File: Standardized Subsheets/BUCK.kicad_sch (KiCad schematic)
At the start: 11 parts, among them U2 TPS562200

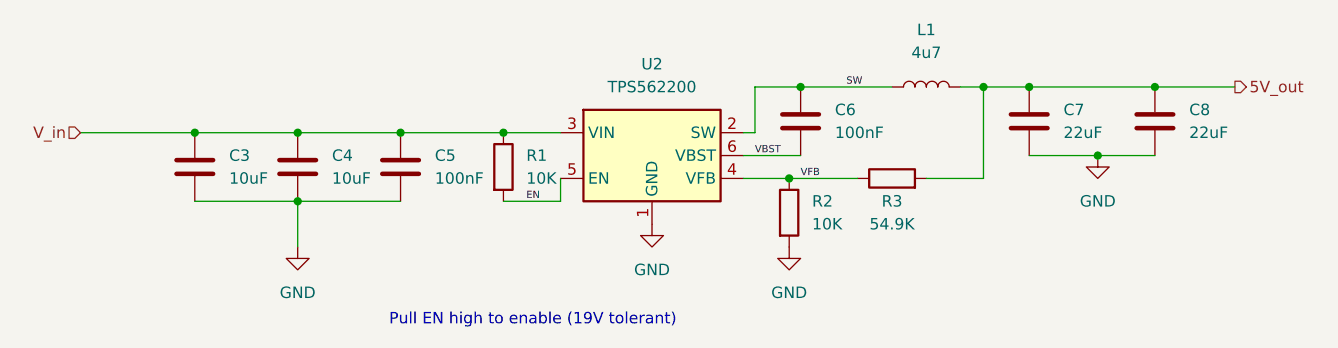
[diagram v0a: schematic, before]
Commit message: Updated VRMs to be 24V compliant
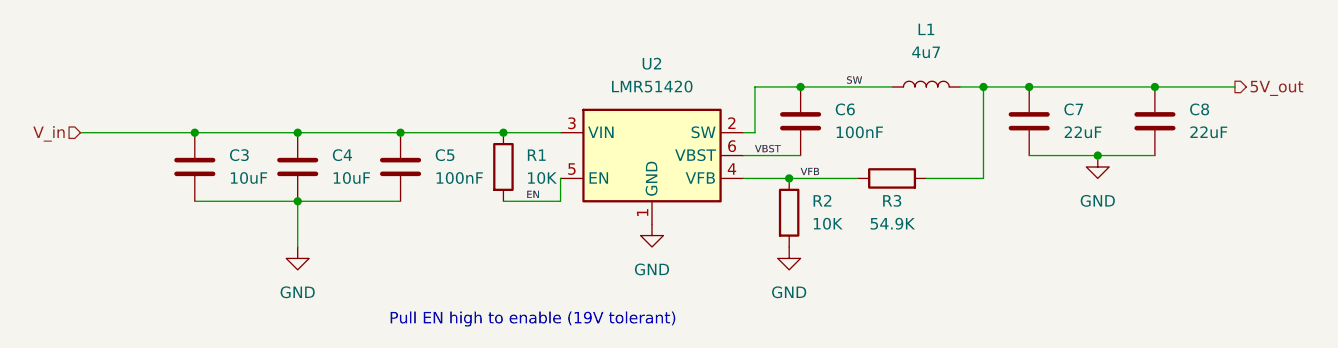
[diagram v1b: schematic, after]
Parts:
- U2: value TPS562200 -> LMR51420
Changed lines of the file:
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@@
     (in_bom yes) (on_board yes) (fields_autoplaced)
     (property "Reference" "U2" (id 0) (at 143.51 71.755 0))
-    (property "Value" "TPS562200" (id 1) (at 143.51 74.295 0))
+    (property "Value" "LMR51420" (id 1) (at 143.51 74.295 0))
     (property "Footprint" "Package_TO_SOT_SMD:SOT-23-6" (id 2) (at 144.78 88.265 0)
       (effects (font (size 1.27 1.27)) (justify left) hide)
     )
-    (property "Datasheet" "http://www.ti.com/lit/ds/symlink/tps563200.pdf" (id 3) (at 143.51 81.915 0)
+    (property "Datasheet" "https://www.ti.com/lit/ds/symlink/lmr51420.pdf?ts=1667094809731&ref_url=https%253A%252F%252Fwww.ti.com%252Fproduct%252FLMR51420" (id 3) (at 143.51 81.915 0)
       (effects (font (size 1.27 1.27)) hide)
     )

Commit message: gitignore
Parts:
- renumbered C3 to C15, C4 to C16, C5 to C17, C6 to C18, C7 to C19, C8 to C20, L1 to L2, R1 to R22, R2 to R23, R3 to R24, U2 to U6
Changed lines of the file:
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@@
     (effects (font (size 1.27 1.27)) (justify right))
   )
-  (symbol (lib_id "Device:C") (at 199.39 78.105 0)
-    (in_bom yes) (on_board yes) (fields_autoplaced)
-    (property "Reference" "C8" (id 0) (at 203.2 76.8349 0)
+  (symbol (lib_id "Device:C") (at 199.39 78.105 0) (unit 1)
+    (in_bom yes) (on_board yes) (fields_autoplaced)
+    (property "Reference" "C20" (id 0) (at 203.2 76.8349 0)
       (effects (font (size 1.27 1.27)) (justify left))
     )
@@
     (pin "2")
   )
-  (symbol (lib_id "power:GND") (at 193.04 81.915 0)
-    (in_bom yes) (on_board yes) (fields_autoplaced)
-    (property "Reference" "#PWR07" (id 0) (at 193.04 88.265 0)
+  (symbol (lib_id "power:GND") (at 193.04 81.915 0) (unit 1)
+    (in_bom yes) (on_board yes) (fields_autoplaced)
+    (property "Reference" "#PWR062" (id 0) (at 193.04 88.265 0)
       (effects (font (size 1.27 1.27)) hide)
     )
@@
     (pin "1")
   )
-  (symbol (lib_id "Device:C") (at 185.42 78.105 0)
-    (in_bom yes) (on_board yes) (fields_autoplaced)
-    (property "Reference" "C7" (id 0) (at 189.23 76.8349 0)
+  (symbol (lib_id "Device:C") (at 185.42 78.105 0) (unit 1)
+    (in_bom yes) (on_board yes) (fields_autoplaced)
+    (property "Reference" "C19" (id 0) (at 189.23 76.8349 0)
       (effects (font (size 1.27 1.27)) (justify left))
     )
@@
     (pin "2")
   )
-  (symbol (lib_id "Device:C") (at 92.71 83.185 0)
-    (in_bom yes) (on_board yes) (fields_autoplaced)
-    (property "Reference" "C3" (id 0) (at 96.52 81.9149 0)
+  (symbol (lib_id "Device:C") (at 92.71 83.185 0) (unit 1)
+    (in_bom yes) (on_board yes) (fields_autoplaced)
+    (property "Reference" "C15" (id 0) (at 96.52 81.9149 0)
       (effects (font (size 1.27 1.27)) (justify left))
     )
@@
     (pin "2")
   )
-  (symbol (lib_id "Device:C") (at 104.14 83.185 0)
-    (in_bom yes) (on_board yes) (fields_autoplaced)
-    (property "Reference" "C4" (id 0) (at 107.95 81.9149 0)
+  (symbol (lib_id "Device:C") (at 104.14 83.185 0) (unit 1)
+    (in_bom yes) (on_board yes) (fields_autoplaced)
+    (property "Reference" "C16" (id 0) (at 107.95 81.9149 0)
       (effects (font (size 1.27 1.27)) (justify left))
     )
@@
     (pin "2")
   )
-  (symbol (lib_id "Device:C") (at 115.57 83.185 0)
-    (in_bom yes) (on_board yes) (fields_autoplaced)
-    (property "Reference" "C5" (id 0) (at 119.38 81.9149 0)
+  (symbol (lib_id "Device:C") (at 115.57 83.185 0) (unit 1)
+    (in_bom yes) (on_board yes) (fields_autoplaced)
+    (property "Reference" "C17" (id 0) (at 119.38 81.9149 0)
       (effects (font (size 1.27 1.27)) (justify left))
     )
@@
     (pin "2")
   )
-  (symbol (lib_id "power:GND") (at 143.51 89.535 0)
-    (in_bom yes) (on_board yes) (fields_autoplaced)
-    (property "Reference" "#PWR05" (id 0) (at 143.51 95.885 0)
+  (symbol (lib_id "power:GND") (at 143.51 89.535 0) (unit 1)
+    (in_bom yes) (on_board yes) (fields_autoplaced)
+    (property "Reference" "#PWR060" (id 0) (at 143.51 95.885 0)
       (effects (font (size 1.27 1.27)) hide)
     )
@@
     (pin "1")
   )
-  (symbol (lib_id "Device:R") (at 170.18 84.455 90)
+  (symbol (lib_id "Device:R") (at 170.18 84.455 90) (unit 1)
     (in_bom yes) (on_board yes)
-    (property "Reference" "R3" (id 0) (at 170.18 86.995 90))
+    (property "Reference" "R24" (id 0) (at 170.18 86.995 90))
     (property "Value" "54.9K" (id 1) (at 170.18 89.535 90))
     (property "Footprint" "Resistor_SMD:R_0603_1608Metric_Pad0.98x0.95mm_HandSolder" (id 2) (at 170.18 86.233 90)
@@
     (pin "2")
   )
-  (symbol (lib_id "Device:R") (at 127 83.185 0)
-    (in_bom yes) (on_board yes) (fields_autoplaced)
-    (property "Reference" "R1" (id 0) (at 129.54 81.9149 0)
+  (symbol (lib_id "Device:R") (at 127 83.185 0) (unit 1)
+    (in_bom yes) (on_board yes) (fields_autoplaced)
+    (property "Reference" "R22" (id 0) (at 129.54 81.9149 0)
       (effects (font (size 1.27 1.27)) (justify left))
     )
@@
     (pin "2")
   )
-  (symbol (lib_id "power:GND") (at 158.75 92.075 0)
-    (in_bom yes) (on_board yes) (fields_autoplaced)
-    (property "Reference" "#PWR06" (id 0) (at 158.75 98.425 0)
+  (symbol (lib_id "power:GND") (at 158.75 92.075 0) (unit 1)
+    (in_bom yes) (on_board yes) (fields_autoplaced)
+    (property "Reference" "#PWR061" (id 0) (at 158.75 98.425 0)
       (effects (font (size 1.27 1.27)) hide)
     )
@@
     (pin "1")
   )
-  (symbol (lib_id "Regulator_Switching:TPS562200") (at 143.51 81.915 0)
-    (in_bom yes) (on_board yes) (fields_autoplaced)
-    (property "Reference" "U2" (id 0) (at 143.51 71.755 0))
+  (symbol (lib_id "Regulator_Switching:TPS562200") (at 143.51 81.915 0) (unit 1)
+    (in_bom yes) (on_board yes) (fields_autoplaced)
+    (property "Reference" "U6" (id 0) (at 143.51 71.755 0))
     (property "Value" "LMR51420" (id 1) (at 143.51 74.295 0))
     (property "Footprint" "Package_TO_SOT_SMD:SOT-23-6" (id 2) (at 144.78 88.265 0)
@@
     (pin "6")
   )
-  (symbol (lib_id "Device:C") (at 160.02 78.105 0)
-    (in_bom yes) (on_board yes) (fields_autoplaced)
-    (property "Reference" "C6" (id 0) (at 163.83 76.8349 0)
+  (symbol (lib_id "Device:C") (at 160.02 78.105 0) (unit 1)
+    (in_bom yes) (on_board yes) (fields_autoplaced)
+    (property "Reference" "C18" (id 0) (at 163.83 76.8349 0)
       (effects (font (size 1.27 1.27)) (justify left))
     )
@@
     (pin "2")
   )
-  (symbol (lib_id "Device:R") (at 158.75 88.265 0)
-    (in_bom yes) (on_board yes) (fields_autoplaced)
-    (property "Reference" "R2" (id 0) (at 161.29 86.9949 0)
+  (symbol (lib_id "Device:R") (at 158.75 88.265 0) (unit 1)
+    (in_bom yes) (on_board yes) (fields_autoplaced)
+    (property "Reference" "R23" (id 0) (at 161.29 86.9949 0)
       (effects (font (size 1.27 1.27)) (justify left))
     )
@@
     (pin "2")
   )
-  (symbol (lib_id "Device:L") (at 173.99 74.295 90)
-    (in_bom yes) (on_board yes) (fields_autoplaced)
-    (property "Reference" "L1" (id 0) (at 173.99 67.945 90))
+  (symbol (lib_id "Device:L") (at 173.99 74.295 90) (unit 1)
+    (in_bom yes) (on_board yes) (fields_autoplaced)
+    (property "Reference" "L2" (id 0) (at 173.99 67.945 90))
     (property "Value" "4u7" (id 1) (at 173.99 70.485 90))
     (property "Footprint" "Inductor_SMD:L_Sunlord_MWSA0518_5.4x5.2mm" (id 2) (at 173.99 74.295 0)
@@
     (pin "2")
   )
-  (symbol (lib_id "power:GND") (at 104.14 92.075 0)
-    (in_bom yes) (on_board yes) (fields_autoplaced)
-    (property "Reference" "#PWR04" (id 0) (at 104.14 98.425 0)
-      (effects (font (size 1.27 1.27)) hide)
-    )
+  (symbol (lib_id "power:GND") (at 104.14 92.075 0) (unit 1)
+    (in_bom yes) (on_board yes) (fields_autoplaced)
+    (property "Reference" "#PWR059" (id 0) (at 104.14 98.425 0)
+      (effects (font (size 1.27 1.27)) hide)
+    )

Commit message: Probably will be breaking everything
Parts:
- renumbered C15 to C1, C16 to C2, C17 to C3, C18 to C4, C19 to C5, C20 to C6, L2 to L1, R22 to R2, R23 to R3, R24 to R4, U6 to U1
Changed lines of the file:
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@@
 (kicad_sch (version 20211123) (generator eeschema)
   (paper "A4")
+  (junction (at 96.52 78.74) (diameter 0) (color 0 0 0 0)
+  )
   (junction (at 158.75 84.455) (diameter 0) (color 0 0 0 0)
   )
@@
     (stroke (width 0) (type default) (color 0 0 0 0))
   )
+  (wire (pts (xy 104.14 78.74) (xy 104.14 79.375))
+    (stroke (width 0) (type default) (color 0 0 0 0))
+  )
   (wire (pts (xy 153.67 81.915) (xy 160.02 81.915))
     (stroke (width 0) (type default) (color 0 0 0 0))
@@
     (stroke (width 0) (type default) (color 0 0 0 0))
   )
+  (wire (pts (xy 92.71 78.74) (xy 92.71 79.375))
+    (stroke (width 0) (type default) (color 0 0 0 0))
+  )
   (wire (pts (xy 153.67 79.375) (xy 154.94 79.375))
     (stroke (width 0) (type default) (color 0 0 0 0))
@@
     (stroke (width 0) (type default) (color 0 0 0 0))
   )
+  (wire (pts (xy 96.52 78.74) (xy 104.14 78.74))
+    (stroke (width 0) (type default) (color 0 0 0 0))
+  )
   (wire (pts (xy 104.14 79.375) (xy 115.57 79.375))
     (stroke (width 0) (type default) (color 0 0 0 0))
@@
     (stroke (width 0) (type default) (color 0 0 0 0))
   )
-  (wire (pts (xy 92.71 79.375) (xy 104.14 79.375))
+  (wire (pts (xy 92.71 78.74) (xy 96.52 78.74))
     (stroke (width 0) (type default) (color 0 0 0 0))
   )
@@
   (symbol (lib_id "Device:C") (at 199.39 78.105 0) (unit 1)
     (in_bom yes) (on_board yes) (fields_autoplaced)
-    (property "Reference" "C20" (id 0) (at 203.2 76.8349 0)
+    (property "Reference" "C6" (id 0) (at 203.2 76.8349 0)
       (effects (font (size 1.27 1.27)) (justify left))
     )
@@
   (symbol (lib_id "power:GND") (at 193.04 81.915 0) (unit 1)
     (in_bom yes) (on_board yes) (fields_autoplaced)
-    (property "Reference" "#PWR062" (id 0) (at 193.04 88.265 0)
+    (property "Reference" "#PWR020" (id 0) (at 193.04 88.265 0)
       (effects (font (size 1.27 1.27)) hide)
     )
@@
   (symbol (lib_id "Device:C") (at 185.42 78.105 0) (unit 1)
     (in_bom yes) (on_board yes) (fields_autoplaced)
-    (property "Reference" "C19" (id 0) (at 189.23 76.8349 0)
+    (property "Reference" "C5" (id 0) (at 189.23 76.8349 0)
       (effects (font (size 1.27 1.27)) (justify left))
     )
@@
   (symbol (lib_id "Device:C") (at 92.71 83.185 0) (unit 1)
     (in_bom yes) (on_board yes) (fields_autoplaced)
-    (property "Reference" "C15" (id 0) (at 96.52 81.9149 0)
+    (property "Reference" "C1" (id 0) (at 96.52 81.9149 0)
       (effects (font (size 1.27 1.27)) (justify left))
     )
@@
   (symbol (lib_id "Device:C") (at 104.14 83.185 0) (unit 1)
     (in_bom yes) (on_board yes) (fields_autoplaced)
-    (property "Reference" "C16" (id 0) (at 107.95 81.9149 0)
+    (property "Reference" "C2" (id 0) (at 107.95 81.9149 0)
       (effects (font (size 1.27 1.27)) (justify left))
     )
@@
   (symbol (lib_id "Device:C") (at 115.57 83.185 0) (unit 1)
     (in_bom yes) (on_board yes) (fields_autoplaced)
-    (property "Reference" "C17" (id 0) (at 119.38 81.9149 0)
+    (property "Reference" "C3" (id 0) (at 119.38 81.9149 0)
       (effects (font (size 1.27 1.27)) (justify left))
     )
@@
   (symbol (lib_id "power:GND") (at 143.51 89.535 0) (unit 1)
     (in_bom yes) (on_board yes) (fields_autoplaced)
-    (property "Reference" "#PWR060" (id 0) (at 143.51 95.885 0)
+    (property "Reference" "#PWR018" (id 0) (at 143.51 95.885 0)
       (effects (font (size 1.27 1.27)) hide)
     )
@@
   (symbol (lib_id "Device:R") (at 170.18 84.455 90) (unit 1)
     (in_bom yes) (on_board yes)
-    (property "Reference" "R24" (id 0) (at 170.18 86.995 90))
+    (property "Reference" "R4" (id 0) (at 170.18 86.995 90))
     (property "Value" "54.9K" (id 1) (at 170.18 89.535 90))
     (property "Footprint" "Resistor_SMD:R_0603_1608Metric_Pad0.98x0.95mm_HandSolder" (id 2) (at 170.18 86.233 90)
@@
   (symbol (lib_id "Device:R") (at 127 83.185 0) (unit 1)
     (in_bom yes) (on_board yes) (fields_autoplaced)
-    (property "Reference" "R22" (id 0) (at 129.54 81.9149 0)
+    (property "Reference" "R2" (id 0) (at 129.54 81.9149 0)
       (effects (font (size 1.27 1.27)) (justify left))
     )
@@
   (symbol (lib_id "power:GND") (at 158.75 92.075 0) (unit 1)
     (in_bom yes) (on_board yes) (fields_autoplaced)
-    (property "Reference" "#PWR061" (id 0) (at 158.75 98.425 0)
+    (property "Reference" "#PWR019" (id 0) (at 158.75 98.425 0)
       (effects (font (size 1.27 1.27)) hide)
     )
@@
   (symbol (lib_id "Regulator_Switching:TPS562200") (at 143.51 81.915 0) (unit 1)
     (in_bom yes) (on_board yes) (fields_autoplaced)
-    (property "Reference" "U6" (id 0) (at 143.51 71.755 0))
+    (property "Reference" "U1" (id 0) (at 143.51 71.755 0))
     (property "Value" "LMR51420" (id 1) (at 143.51 74.295 0))
     (property "Footprint" "Package_TO_SOT_SMD:SOT-23-6" (id 2) (at 144.78 88.265 0)
@@
   (symbol (lib_id "Device:C") (at 160.02 78.105 0) (unit 1)
     (in_bom yes) (on_board yes) (fields_autoplaced)
-    (property "Reference" "C18" (id 0) (at 163.83 76.8349 0)
+    (property "Reference" "C4" (id 0) (at 163.83 76.8349 0)
       (effects (font (size 1.27 1.27)) (justify left))
     )
@@
   (symbol (lib_id "Device:R") (at 158.75 88.265 0) (unit 1)
     (in_bom yes) (on_board yes) (fields_autoplaced)
-    (property "Reference" "R23" (id 0) (at 161.29 86.9949 0)
+    (property "Reference" "R3" (id 0) (at 161.29 86.9949 0)
       (effects (font (size 1.27 1.27)) (justify left))
     )
@@
     (pin "2")
   )
+  (symbol (lib_id "power:PWR_FLAG") (at 96.52 78.74 0) (unit 1)
+    (in_bom yes) (on_board yes) (fields_autoplaced)
+    (property "Reference" "#FLG0101" (id 0) (at 96.52 76.835 0)
+      (effects (font (size 1.27 1.27)) hide)
+    )
+    (property "Value" "PWR_FLAG" (id 1) (at 96.52 75.1355 0))
+    (property "Footprint" "" (id 2) (at 96.52 78.74 0)
+      (effects (font (size 1.27 1.27)) hide)
+    )
+    (property "Datasheet" "~" (id 3) (at 96.52 78.74 0)
+      (effects (font (size 1.27 1.27)) hide)
+    )
+    (pin "1")
+  )
   (symbol (lib_id "Device:L") (at 173.99 74.295 90) (unit 1)
     (in_bom yes) (on_board yes) (fields_autoplaced)
-    (property "Reference" "L2" (id 0) (at 173.99 67.945 90))
+    (property "Reference" "L1" (id 0) (at 173.99 67.945 90))
     (property "Value" "4u7" (id 1) (at 173.99 70.485 90))
     (property "Footprint" "Inductor_SMD:L_Sunlord_MWSA0518_5.4x5.2mm" (id 2) (at 173.99 74.295 0)
@@
   (symbol (lib_id "power:GND") (at 104.14 92.075 0) (unit 1)
     (in_bom yes) (on_board yes) (fields_autoplaced)
-    (property "Reference" "#PWR059" (id 0) (at 104.14 98.425 0)
-      (effects (font (size 1.27 1.27)) hide)
-    )
+    (property "Reference" "#PWR017" (id 0) (at 104.14 98.425 0)
+      (effects (font (size 1.27 1.27)) hide)
+    )
